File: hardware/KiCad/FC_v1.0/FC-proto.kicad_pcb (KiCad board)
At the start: 4 copper layers, 56 x 46 mm, 121 parts, among them J1 SM06B-GHS-TB, J10 PAD_OUT, J2 MEM2061-01-188-00-A, J3 USB4105-GF-A, J4 Conn_ARM_SWD_TagConnect_TC203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, J5 SM06B-GHS-TB, J6 SM06B-GHS-TB, J7 SM04B-GHS-TB, J8 SM06B-GHS-TB, J9 PAD_OUT, Q1 AO3400A, SW1 PCM12SMTRFC, U1 STM32H743ZIT6, U2 TPS2113ADRBR, U3 TPS62130ARGTR, U4 TPS7A2133PQWDRBRQ1, U5 ICM-40609-D, U6 MMC5983MA, U7 BMP390, U8 USBLC6-2SC6, Y2 16MHz

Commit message: FC design v0.5 corrected
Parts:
- added C46: 1u, Capacitor_SMD:C_0402_1005Metric, F.Cu at (85.0, 116.5)
- added C47: 1u, Capacitor_SMD:C_0402_1005Metric, F.Cu at (105.0, 84.2)
- added C48: 1u, Capacitor_SMD:C_0402_1005Metric, F.Cu at (96.5, 116.5)
- added C49: 1u, Capacitor_SMD:C_0402_1005Metric, F.Cu at (72.0, 104.8)
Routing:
- net +3.3V: track 136.9 -> 60.3 mm
- net +3.3VA: track 49.0 -> 14.1 mm
- net VBUS: track 35.1 -> 11.7 mm
- net GND: vias 121 -> 119
- added copper zone on In2.Cu, net +3.3V
- added copper zone on In2.Cu, net +3.3VA
- added copper zone on In2.Cu, net +5V
- added copper zone on In2.Cu, net VBUS

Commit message: Complete Routing
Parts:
- removed the R5 at (96.0, 115.0)
- removed the R6 at (97.0, 115.0)
- added C14: 100n, Capacitor_SMD:C_0402_1005Metric, F.Cu at (83.8, 96.2)
- added C46: 1u, Capacitor_SMD:C_0402_1005Metric, F.Cu at (89.5, 83.5)
- added J12: PAD_OUT_Mini, FC-FootprintLib:Mini_Pad_out_1x6, B.Cu at (108.5, 120.6)
- added J13: PAD_OUT_Mini, FC-FootprintLib:Mini_Pad_out_1x6, B.Cu at (95.0, 120.6)
- added J6: SM04B-GHS-TB, FC-FootprintLib:CONN_SM04B-GHS-TB_JST, F.Cu at (86.2, 80.0)
- added R31: 43k, Resistor_SMD:R_0402_1005Metric, F.Cu at (122.0, 87.2)
- added R32: 82k, Resistor_SMD:R_0402_1005Metric, F.Cu at (124.0, 87.2)
- added R38: 4.7k, Resistor_SMD:R_0402_1005Metric, F.Cu at (95.0, 83.5)
- added R39: 4.7k, Resistor_SMD:R_0402_1005Metric, F.Cu at (98.5, 83.5)
- added R40: 4.7k, Resistor_SMD:R_0402_1005Metric, F.Cu at (97.8, 114.5)
- added R41: 4.7k, Resistor_SMD:R_0402_1005Metric, F.Cu at (95.8, 114.5)
- C48: renamed from C47; value 1u -> 10u; footprint Capacitor_SMD:C_0402_1005Metric -> Capacitor_SMD:C_0603_1608Metric
- C49: value 1u -> 10u; footprint Capacitor_SMD:C_0402_1005Metric -> Capacitor_SMD:C_0603_1608Metric
- R10: renamed from R12; value 100 -> 33
- R6: renamed from R8; value 47 -> 33
- R7: renamed from R9; value 100 -> 33
- R8: renamed from R10; value 100 -> 33
- R9: renamed from R11; value 100 -> 33
- moved J11 22.1 mm to (73.5, 90.0), turned to -90 degrees
- moved J10 22.1 mm to (70.5, 90.0), turned to -90 degrees
- moved C48 10.6 mm to (115.0, 80.8), turned to 90 degrees
- moved R30 6.88 mm to (108.8, 86.0)
- moved J8 6.50 mm to (108.5, 80.0)
- moved R13 6.49 mm to (115.5, 85.5), turned to 180 degrees
- moved C42 6.28 mm to (107.2, 85.5), turned to -90 degrees
- moved R12 5.80 mm to (115.7, 84.5), turned to 180 degrees
- moved J9 5.75 mm to (96.8, 80.0)
- moved R11 5.35 mm to (115.5, 83.5), turned to 180 degrees
- moved C22 4.09 mm to (111.0, 84.5), turned to 180 degrees
- moved C49 3.88 mm to (72.1, 100.9)
- moved SW1 3.78 mm to (86.2, 79.5)
- moved R1 3.74 mm to (86.5, 84.8), turned to 0 degrees
- moved C47 3.18 mm to (82.8, 118.8), turned to -90 degrees
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- renumbered C16 to C15, C17 to C16, C18 to C17, C19 to C18, C20 to C19, C21 to C20, C22 to C21, C23 to C22, C24 to C23, C25 to C24, C26 to C25, C27 to C26, C28 to C27, C29 to C28, C30 to C29, C31 to C30, C32 to C31, C33 to C32, C34 to C33, C35 to C34, C36 to C35, C37 to C36, C38 to C37, C39 to C38, C40 to C39, C41 to C40, C42 to C41, C43 to C42, C44 to C43, C45 to C44, C48 to C45, C46 to C47, J9 to J10, J10 to J11, J8 to J5, J5 to J7, J6 to J8, J7 to J9, R13 to R11, R14 to R12, R15 to R13, R16 to R14, R17 to R15, R18 to R16, R19 to R17, R20 to R18, R21 to R19, R22 to R20, R23 to R21, R24 to R22, R25 to R23, R26 to R24, R27 to R25, R28 to R26, R29 to R27, R30 to R28, R31 to R29, R32 to R30, R38 to R42, R7 to R5
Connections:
- net Net-(L1-Pad2) renamed /Power Section/SW_L
- J10 pad 3: PO_SCL -> PO_TX
- J10 pad 4: PO_SDA -> PO_RX
- J10 pad 5: PO_TX -> PO_SCL
- J10 pad 6: PO_RX -> PO_SDA
- R4 pad 1: Net-(U1-PG0) -> Net-(U1-PD6)
- U1 pad 101: unconnected-(U1-PA9-Pad101) -> USB_VBUS_SENSE
- U1 pad 110: CDS_SD -> unconnected-(U1-PA15-Pad110)
- U1 pad 117: unconnected-(U1-PD3-Pad117) -> CDS_SD
- U1 pad 122: unconnected-(U1-PD6-Pad122) -> Net-(U1-PD6)
- U1 pad 125: SWITCH -> unconnected-(U1-PG10-Pad125)
- U1 pad 127: BUZZ -> unconnected-(U1-PG12-Pad127)
- U1 pad 2: unconnected-(U1-PE3-Pad2) -> SWITCH
- U1 pad 29: unconnected-(U1-PC3_C-Pad29) -> BUZZ
- U1 pad 36: unconnected-(U1-PA2-Pad36) -> PO_TX
- U1 pad 37: unconnected-(U1-PA3-Pad37) -> PO_RX
- U1 pad 44: unconnected-(U1-PC4-Pad44) -> ADC_IN2
- U1 pad 47: unconnected-(U1-PB1-Pad47) -> ADC_IN3
- U1 pad 53: unconnected-(U1-PF13-Pad53) -> ADC_IN1
- U1 pad 54: Net-(U1-PF14) -> PO_SCL
- U1 pad 55: Net-(U1-PF15) -> PO_SDA
- U1 pad 56: Net-(U1-PG0) -> unconnected-(U1-PG0-Pad56)
- U1 pad 73: PO_RX -> UART5_RX
- U1 pad 74: PO_TX -> UART5_TX
- U1 pad 78: unconnected-(U1-PD9-Pad78) -> PWR_GOOD
- U1 pad 96: unconnected-(U1-PC6-Pad96) -> RC_TX
- U1 pad 97: unconnected-(U1-PC7-Pad97) -> RC_RX
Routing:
- net BAT_CURRENT: track 2.30 -> 49.4 mm, vias 1 -> 2
- net BAT_VOLTAGE: track 2.30 -> 49.2 mm, vias 1 -> 2
- net BUZZ: track 0.00 -> 39.7 mm, vias 0 -> 2
- net RGB_LED_R: track 0.00 -> 37.9 mm, vias 0 -> 2
- net RGB_LED_G: track 0.00 -> 36.4 mm, vias 0 -> 2
- net PO_SCL: track 0.00 -> 34.9 mm, vias 0 -> 1
- net RGB_LED_B: track 0.00 -> 34.7 mm, vias 0 -> 2
- net RC_RX: track 0.00 -> 34.0 mm, vias 0 -> 2
- net PO_SDA: track 0.00 -> 33.7 mm, vias 0 -> 1
- net RC_TX: track 0.00 -> 33.7 mm, vias 0 -> 2
- net SWITCH: track 2.77 -> 35.5 mm, vias 0 -> 2
- net +5V: track 16.3 -> 48.2 mm, vias 0 -> 10
- net GPS_TX: track 0.00 -> 31.2 mm, vias 0 -> 4
- net GPS_CAN_TX: track 0.00 -> 29.4 mm, vias 0 -> 2
- net USB_VBUS_SENSE: track 0.00 -> 27.6 mm, vias 0 -> 2
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- added copper zone on In2.Cu, net +5V_SYS
- added copper zone on F.Cu, net /Power Section/Buck_Out

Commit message: Top/Bot pours
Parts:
- J12, J13: footprint FC-FootprintLib:Mini_Pad_out_1x6 -> FC-FootprintLib:Pad_out_mini_1x4
- moved J12 8.51 mm to (100.0, 121.0)
- moved J13 4.02 mm to (91.0, 121.0)
- moved C48 0.15 mm to (115.0, 80.9)
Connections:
- J12 pad 3: unconnected-(J12-Pin_3-Pad3) -> GPIO_68
- J12 pad 4: unconnected-(J12-Pin_4-Pad4) -> GPIO_69
- J13 pad 1: ADC_IN1 -> GPIO_70
- J13 pad 2: ADC_IN3 -> ADC_IN2
- J13 pad 3: ADC_IN2 -> ADC_IN3
- J13 pad 4: unconnected-(J13-Pin_4-Pad4) -> ADC_IN1
- U1 pad 68: unconnected-(U1-PE15-Pad68) -> GPIO_68
- U1 pad 69: unconnected-(U1-PB10-Pad69) -> GPIO_69
- U1 pad 70: unconnected-(U1-PB11-Pad70) -> GPIO_70
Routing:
- net ADC_IN2: track 0.00 -> 23.6 mm, vias 0 -> 1
- net GPIO_70: track 0.00 -> 23.5 mm, vias 0 -> 1
- net GPIO_69: track 0.00 -> 22.4 mm, vias 0 -> 1
- net ADC_IN3: track 0.00 -> 22.0 mm, vias 0 -> 1
- net GPIO_68: track 0.00 -> 20.7 mm, vias 0 -> 1
- net ADC_IN1: track 0.00 -> 19.8 mm, vias 0 -> 1
- net UART5_TX: track 0.00 -> 19.6 mm, vias 0 -> 3
- net UART5_RX: track 0.00 -> 18.2 mm, vias 0 -> 3
- net GND: track 131.1 -> 119.8 mm, vias 102 -> 137
- net VBUS: track 11.7 -> 1.90 mm
- net /Power Section/SW_L: track 11.4 -> 3.02 mm
- net +5V: track 48.2 -> 41.4 mm, vias 10 -> 11
- net PO_SDA: track 33.7 -> 38.2 mm
- net PO_SCL: track 34.9 -> 38.5 mm
- net /Power Section/Buck_Out: track 16.9 -> 19.8 mm
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- added copper zone on F.Cu, net +5V
- added copper zone on F.Cu, net /Power Section/SW_L
- added copper zone on B.Cu, net GND
- added copper zone on F.Cu, net GND
- added copper zone on F.Cu, net VBUS

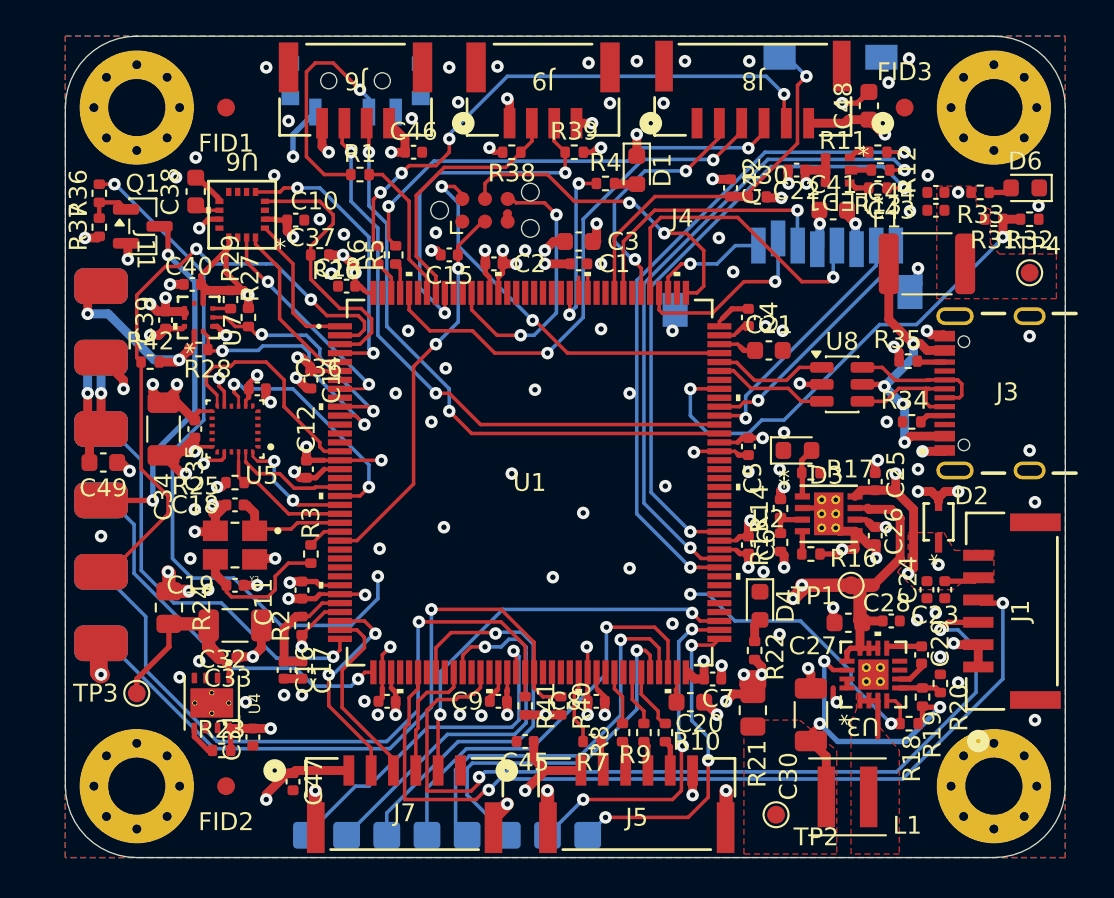
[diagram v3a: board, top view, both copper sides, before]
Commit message: Silkscreen improvements
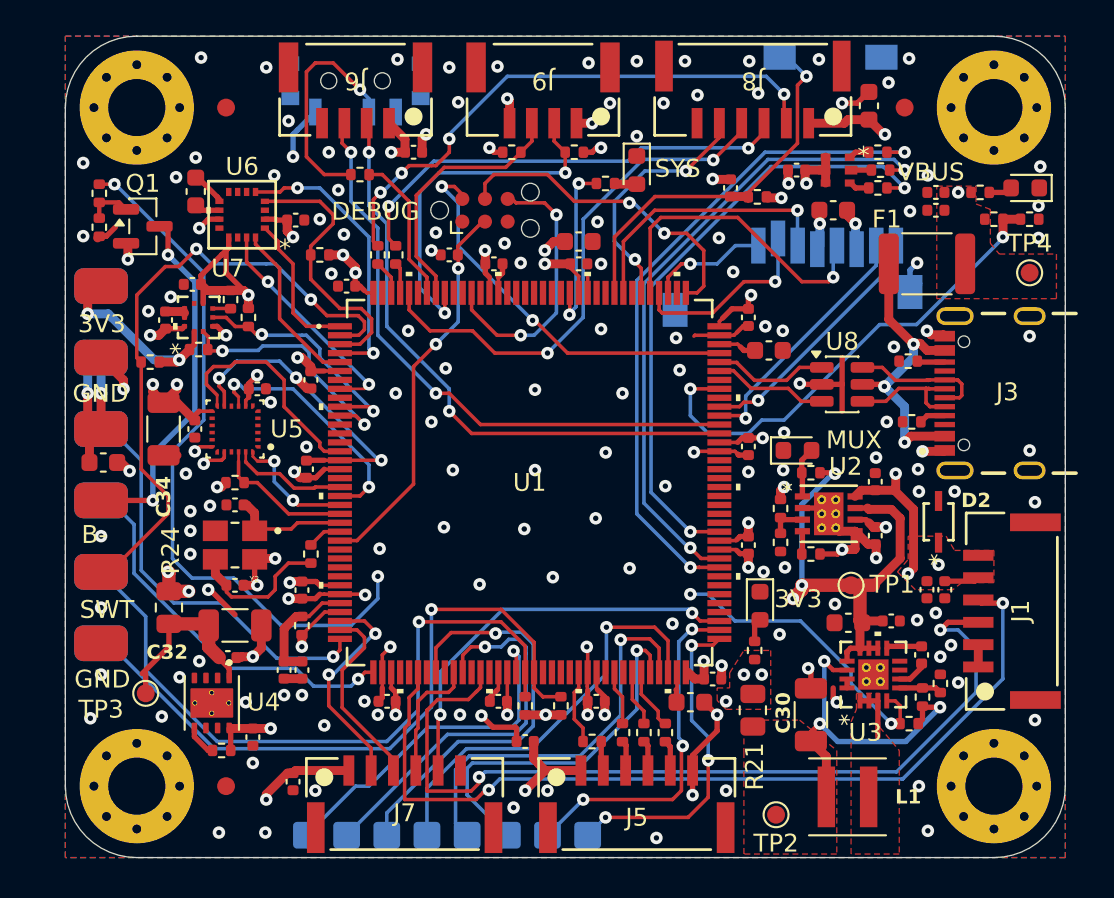
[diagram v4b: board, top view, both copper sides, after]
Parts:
- moved TP3 0.50 mm to (74.5, 113.8)
- renumbered LED1 to LED
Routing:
- net +5V_SYS: track 22.8 -> 30.8 mm, vias 3 -> 4
- net GND: track 119.8 -> 112.8 mm, vias 137 -> 159
- net +3.3V: track 82.1 -> 75.3 mm, vias 30 -> 31
- added copper zone on F.Cu, net +3.3V
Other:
- board text added: "3V3"
- board text added: "5V"
- board text added: "B-"
- board text added: "DEBUG"
- board text added: "GND"
- board text added: "MUX"
- board text added: "RX"
- board text added: "SCL"
- board text added: "SDA"
- board text added: "SWT"
- board text added: "SYS"
- board text added: "TX"
- board text added: "VBUS"

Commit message: Silkscreen Finish
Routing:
- net BUZZ: track 39.7 -> 41.9 mm
- net GND: vias 159 -> 162
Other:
- board text added: "// FC Dev Board // v0.7 // G.A, S.B"
- board text added: "ADC_IN1"
- board text added: "ADC_IN2"
- board text added: "ADC_IN3"
- board text added: "BOOT"
- board text added: "GPIO_68"
- board text added: "GPIO_69"
- board text added: "GPIO_70"
- board text added: "Shirley"
- board text added: "UART5_RX"
- board text added: "UART5_TX"
- board text added: "X"
- board text added: "Y"
- board text added: "Z"

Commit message: Silkscreen Finish*
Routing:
- net +3.3V: track 75.3 -> 77.0 mm
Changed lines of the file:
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@@
+	)
+	(segment
+		(start 91.615 88)
+		(end 92.23 87.385)
+		(width 0.3)
+		(layer "F.Cu")
+		(net 2)
 	)
 	(segment
@@
 		(width 0.3)
 		(layer "F.Cu")
+		(net 2)
+	)
+	(segment
+		(start 90.75 88)
+		(end 91.615 88)
+		(width 0.3)
+		(layer "F.Cu")

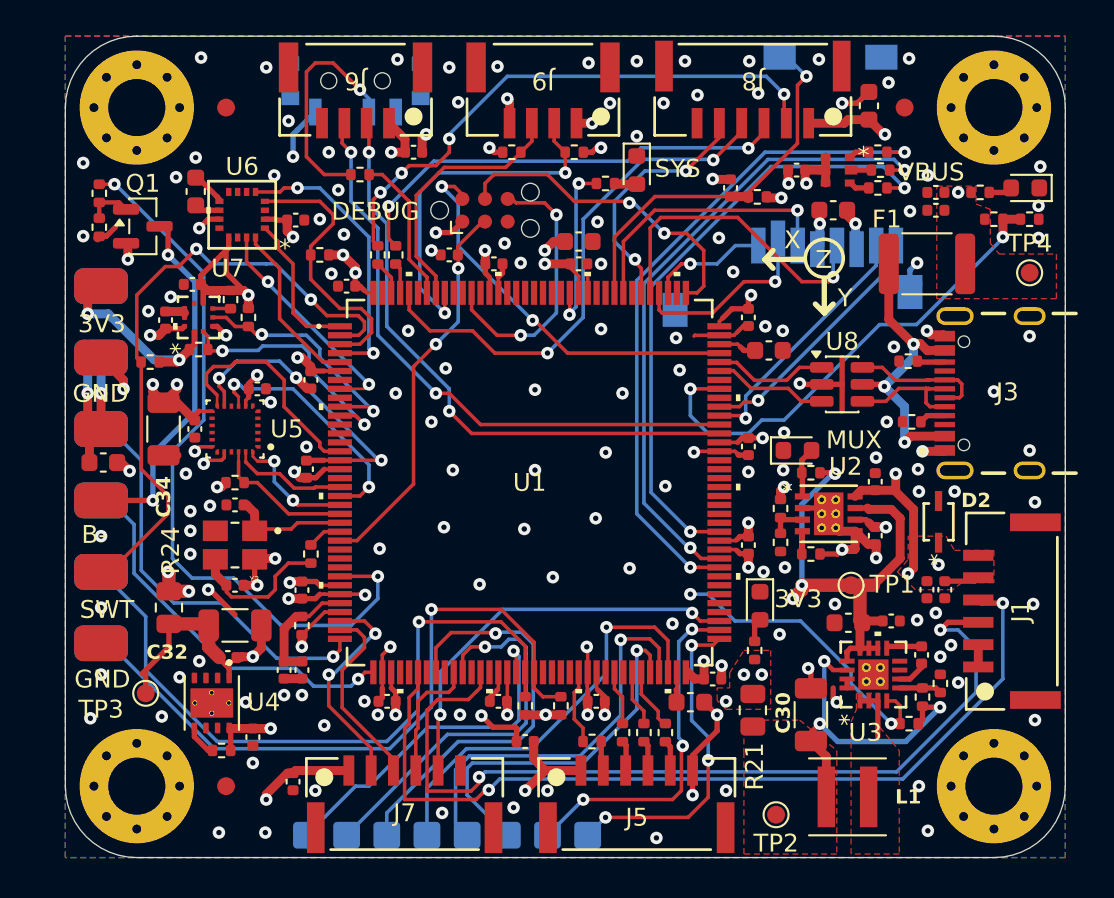
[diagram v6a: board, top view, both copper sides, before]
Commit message: Pinout / DRC check
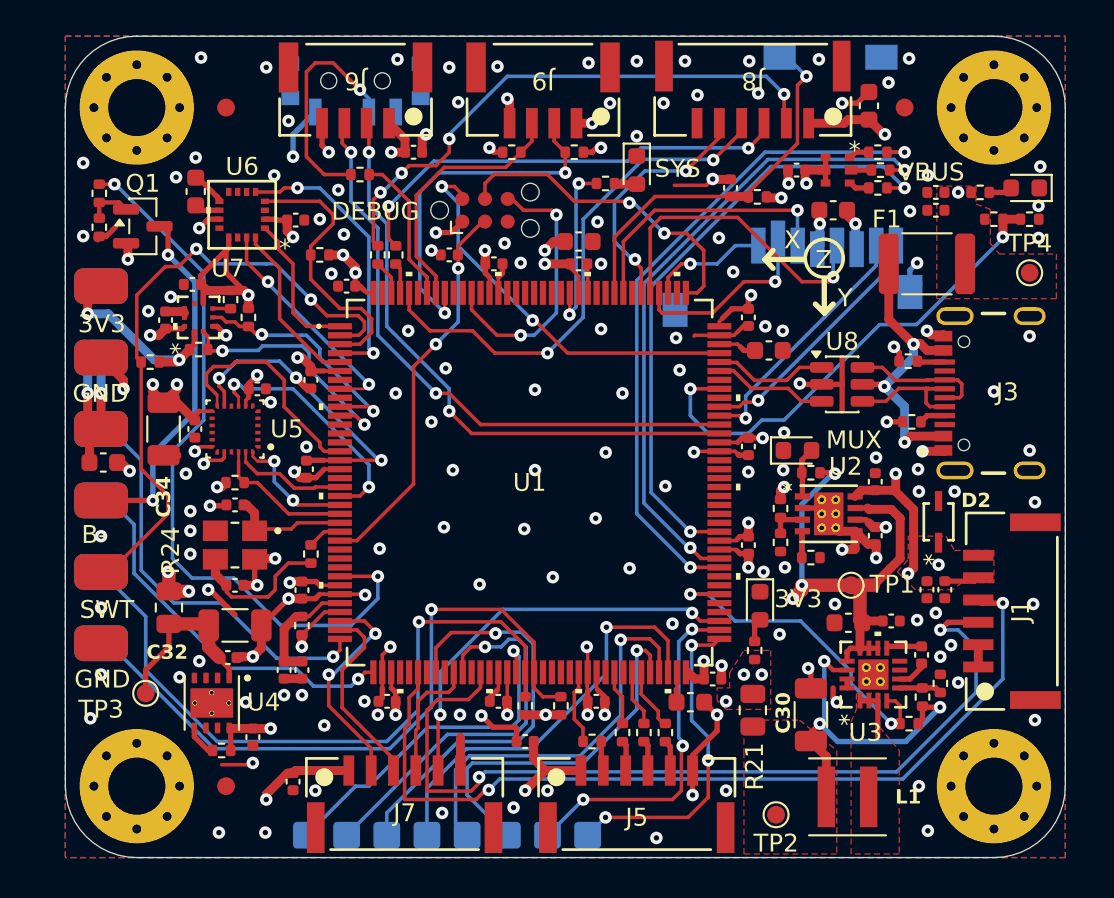
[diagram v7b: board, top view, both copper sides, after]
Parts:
- moved R16 0.20 mm to (111.8, 106.2)
- renumbered LED to LED1
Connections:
- net CDS_SD renamed SD_CDS
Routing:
- net GND: track 112.8 -> 125.6 mm, vias 162 -> 161
- net +5V: track 41.4 -> 51.0 mm
- net +3.3V: track 77.0 -> 82.2 mm
- net PWR_GOOD: track 17.0 -> 18.6 mm
